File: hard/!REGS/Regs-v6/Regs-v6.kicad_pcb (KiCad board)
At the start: 2 copper layers, 160 x 99.1 mm, 60 parts, among them J1 Conn_01x15_Female, J10 Conn_01x01_Male, J11 Conn_01x03_Male, J12 Conn_01x01_Male, J13 Conn_01x01_Male, J14 Conn_01x01_Male, J15 Conn_01x01_Male, J16 Screw_Terminal_01x02, J17 Conn_01x09_Male, J18 Conn_01x09_Male, J19 Conn_01x01_Male, J2 Conn_01x15_Female, J20 Conn_01x01_Male, J21 Conn_01x01_Male, J22 Conn_01x01_Male, J23 Conn_01x01_Male, J24 Conn_01x01_Male, J3 Conn_01x15_Female, J4 Conn_01x15_Female, J5 Conn_01x15_Female, J6 Conn_01x15_Female, J7 Conn_01x15_Female, J8 Conn_01x15_Female, J9 Conn_01x01_Male, Q1 IRLML5203, U1 REG_CNT, U10 REG_CNT, U11 REG_CNT, U12 REG_CNT, U13 74LS139, U14 74HC00, U15 MUX2-1, U16 REG_CNT, U17 REG_CNT, U18 REG_CNT, U19 REG_CNT, U2 REG_CNT, U3 REG_CNT, U4 REG_CNT, U5 REG_CNT, U6 REG_CNT, U7 REG_CNT, U8 REG_CNT, U9 REG_CNT

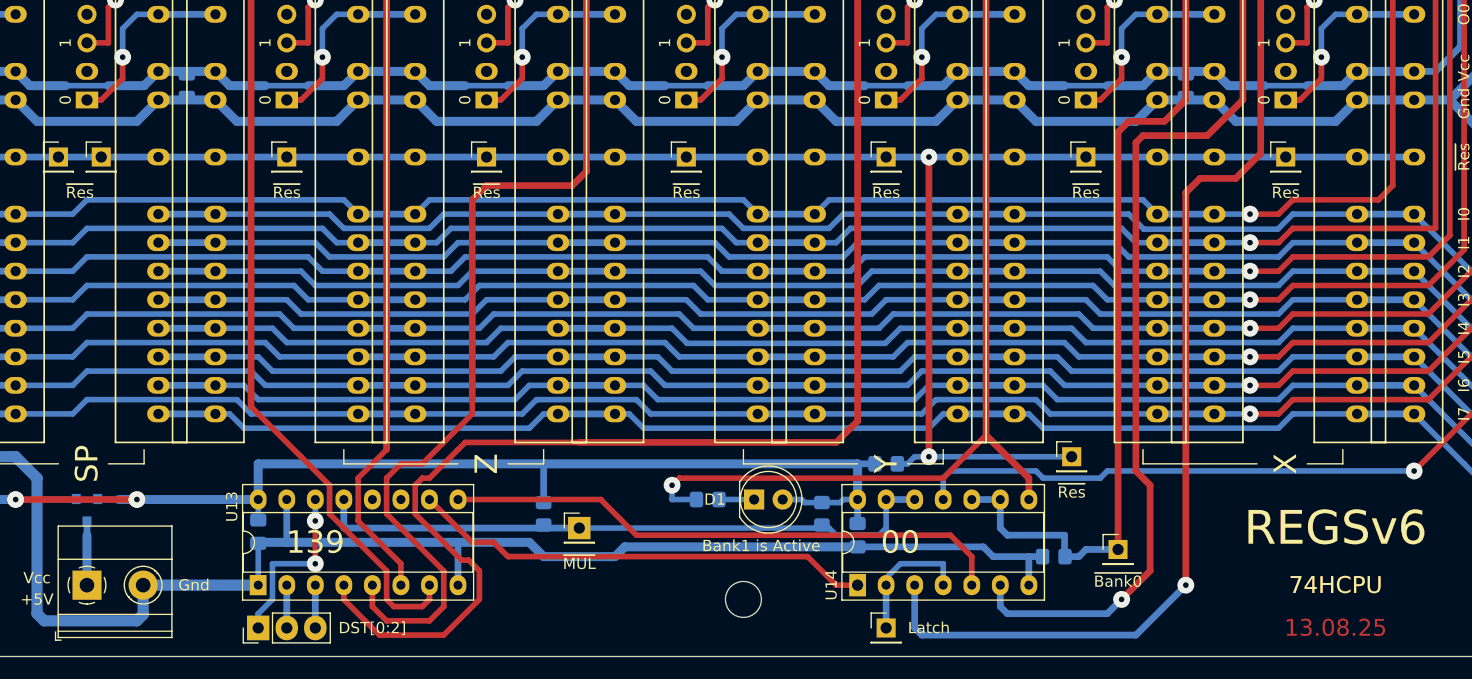
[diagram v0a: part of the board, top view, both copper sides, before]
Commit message: Fix label name
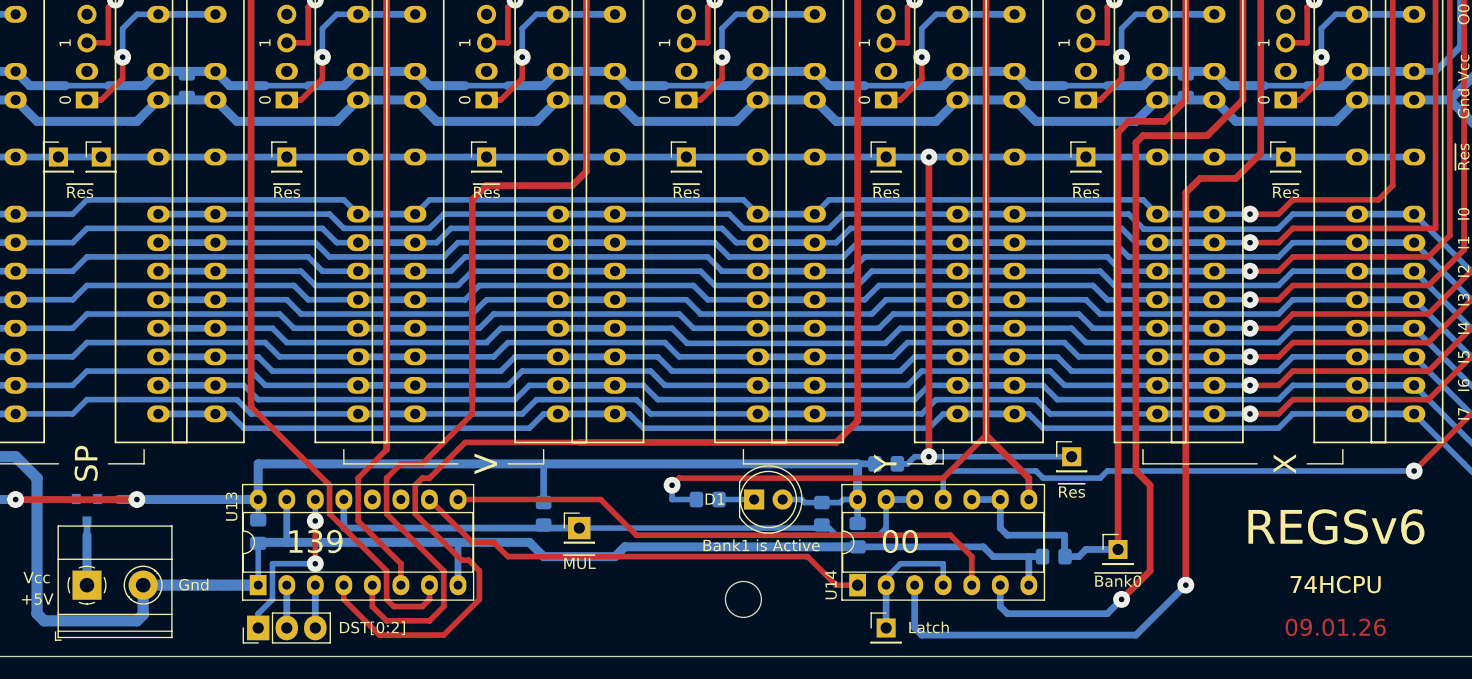
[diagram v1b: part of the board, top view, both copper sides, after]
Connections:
- net /~Bank0 renamed /~{Bank0}
- net /~Bank1 renamed /~{Bank1}
- net /~H renamed /~{H}
- net /~L renamed /~{L}
- net /~MUL renamed /~{MUL}
- net /~R0 renamed /~{R0}
- net /~R1 renamed /~{R1}
- net /~R2 renamed /~{R2}
- net /~R3 renamed /~{R3}
- net /~Res renamed /~{Res}
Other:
- net class Default removed
- board text added: "09.01.26"
- board text added: "V"
- board text added: "~{Bank0}"
- board text added: "~{CS}"
- board text added: "~{Col}"
- board text added: "~{MUL}"
- board text added: "~{Res}"
- board text added: "~{Row}"
- board text removed: "13.08.25"
- board text removed: "Z"
- board text removed: "~Bank0"
- board text removed: "~CS"
- board text removed: "~Col"
- board text removed: "~MUL"
- board text removed: "~Res"
- board text removed: "~Row"

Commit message: Regs v6.1
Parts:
- added J2: Conn_01x22_Socket, Connector_PinSocket_2.54mm:PinSocket_1x22_P2.54mm_Vertical, F.Cu at (183.5, 21.6)
- added J3: Conn_01x22_Socket, Connector_PinSocket_2.54mm:PinSocket_1x22_P2.54mm_Vertical, F.Cu at (188.0, 23.7)
- added J4: Conn_01x22_Socket, Connector_PinSocket_2.54mm:PinSocket_1x22_P2.54mm_Vertical, F.Cu at (192.6, 23.7)
- added J5: Conn_01x22_Socket, Connector_PinSocket_2.54mm:PinSocket_1x22_P2.54mm_Vertical, F.Cu at (197.2, 23.7)
- added J6: Conn_01x22_Socket, Connector_PinSocket_2.54mm:PinSocket_1x22_P2.54mm_Vertical, F.Cu at (201.8, 23.7)
- added J7: Conn_01x22_Socket, Connector_PinSocket_2.54mm:PinSocket_1x22_P2.54mm_Vertical, F.Cu at (206.4, 23.7)
- added J8: Conn_01x22_Socket, Connector_PinSocket_2.54mm:PinSocket_1x22_P2.54mm_Vertical, F.Cu at (211.0, 23.7)
- J1: value Conn_01x15_Female -> Conn_01x22_Socket; footprint Connector_PinSocket_2.54mm:PinSocket_1x15_P2.54mm_Vertical -> Connector_PinSocket_2.54mm:PinSocket_1x22_P2.54mm_Vertical
- moved J1 8.89 mm to (141.0, 71.1)
- moved J10 2.54 mm to (143.5, 67.3)
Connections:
- J1 pad 10: Net-(J1-Pad10) -> /R0.3
- J1 pad 11: /R0.5 -> unconnected-(J1-Pin_11-Pad11)
- J1 pad 12: Net-(J1-Pad12) -> unconnected-(J1-Pin_12-Pad12)
- J1 pad 13: /R0.6 -> /R0.4
- J1 pad 14: Net-(J1-Pad14) -> unconnected-(J1-Pin_14-Pad14)
- J1 pad 15: /R0.7 -> unconnected-(J1-Pin_15-Pad15)
- J1 pad 2: Net-(J1-Pad2) -> unconnected-(J1-Pin_2-Pad2)
- J1 pad 3: /R0.1 -> unconnected-(J1-Pin_3-Pad3)
- J1 pad 4: Net-(J1-Pad4) -> /R0.1
- J1 pad 5: /R0.2 -> unconnected-(J1-Pin_5-Pad5)
- J1 pad 6: Net-(J1-Pad6) -> unconnected-(J1-Pin_6-Pad6)
- J1 pad 7: /R0.3 -> /R0.2
- J1 pad 8: Net-(J1-Pad8) -> unconnected-(J1-Pin_8-Pad8)
- J1 pad 9: /R0.4 -> unconnected-(J1-Pin_9-Pad9)
- U13 pad 11: Net-(U13-Pad11) -> unconnected-(U13B-O1-Pad11)
- U13 pad 12: Net-(U13-Pad12) -> unconnected-(U13B-O0-Pad12)
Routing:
- net /R0.0: track 17.2 -> 26.5 mm, vias 1 -> 0
- net /R0.7: track 19.4 -> 27.9 mm, vias 1 -> 0
- net /R0.6: track 17.2 -> 23.9 mm, vias 1 -> 0
- net /R0.1: track 15.4 -> 20.6 mm, vias 1 -> 0
- net /R0.2: track 12.5 -> 15.5 mm, vias 1 -> 0
- net /R0.5: track 15.4 -> 18.1 mm, vias 1 -> 0
- net /~{Bank0}: track 259.5 -> 260.6 mm
- net VCC: track 326.4 -> 327.4 mm
- net /~{L}: track 233.1 -> 232.5 mm
- net /~{R0}: track 191.1 -> 191.6 mm
- net /R0.4: track 12.5 -> 13.0 mm, vias 1 -> 0
- net /R0.3: track 11.4 -> 12.0 mm, vias 1 -> 0
- net GND: track 402.3 -> 402.8 mm
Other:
- board text added: "23.02.26"
- board text added: "REGSv6.1"
- board text removed: "09.01.26"
- board text removed: "REGSv6"

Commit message: Regs v6.1 in work
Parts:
- removed the J2 at (123.2, 62.2)
- removed the J3 at (105.4, 62.2)
- removed the J4 at (87.6, 62.2)
- removed the J5 at (69.8, 62.2)
- removed the J6 at (52.1, 62.2)
- removed the J7 at (34.3, 62.2)
- removed the J8 at (16.5, 62.2)
- J2, J3, J4, J5, J6, J7, J8: moved to B.Cu
- moved J8 201.8 mm to (16.5, 77.5)
- moved J7 180.3 mm to (34.3, 77.5)
- moved J6 159.1 mm to (52.1, 77.5)
- moved J5 138.3 mm to (69.8, 77.5)
- moved J4 117.9 mm to (87.6, 77.5)
- moved J11 116.9 mm to (62.2, -6.97), turned to -90 degrees
- moved U13 109.3 mm to (62.2, -3.17), turned to -90 degrees
- moved R5 103.2 mm to (36.8, 3.19), turned to -90 degrees
- moved C3 99.9 mm to (62.2, 1.60), turned to 90 degrees
- moved J3 98.6 mm to (105.4, 77.5)
- moved J2 82.2 mm to (123.2, 77.5)
- moved J15 44.4 mm to (61.0, 109.2)
- moved J14 40.6 mm to (85.6, 105.8)
- moved R7 38.7 mm to (81.8, 106.2), turned to -90 degrees
- moved R6 36.5 mm to (69.2, 99.7)
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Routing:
- net GND: track 402.8 -> 298.9 mm
- net /~{Bank0}: track 260.6 -> 179.8 mm, vias 13 -> 10
- net VCC: track 327.4 -> 247.8 mm
- net /~{R0}: track 191.6 -> 124.2 mm
- net /~{R1}: track 148.3 -> 87.6 mm
- net /~{H}: track 220.9 -> 164.3 mm, vias 2 -> 1
- net Net-(U15-S): track 116.4 -> 61.0 mm, vias 1 -> 0
- net Net-(U13B-O3): track 50.4 -> 2.54 mm
- net /~{L}: track 232.5 -> 194.5 mm, vias 2 -> 1
- net Net-(U13B-O2): track 41.3 -> 5.50 mm
- net /~{R3}: track 119.7 -> 95.0 mm
- net /H7: track 174.8 -> 159.5 mm
- net /L6: track 138.6 -> 124.2 mm
- net /L5: track 138.6 -> 124.2 mm
- net /L4: track 138.6 -> 124.3 mm
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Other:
- board text added: "Добавить конденсаторов между каждой парой регистров!"

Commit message: Regs-v6.1 in work
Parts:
- moved J21 0.63 mm to (108.0, 73.7)
- moved J23 0.63 mm to (125.7, 73.7)
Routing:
- net /R1.0: track 13.2 -> 26.5 mm, vias 1 -> 0
- net /H3: track 166.9 -> 179.6 mm
- net /R3.7: track 16.8 -> 27.9 mm, vias 1 -> 0
- net /R2.7: track 16.8 -> 27.9 mm, vias 1 -> 0
- net /R1.7: track 16.8 -> 27.9 mm, vias 1 -> 0
- net /R2.6: track 12.6 -> 23.5 mm, vias 1 -> 0
- net /H4: track 168.7 -> 179.6 mm
- net /R2.0: track 15.9 -> 26.5 mm, vias 1 -> 0
- net /H5: track 170.5 -> 179.6 mm
- net /R2.5: track 9.42 -> 18.5 mm, vias 1 -> 0
- net /R3.6: track 15.9 -> 23.5 mm, vias 1 -> 0
- net /R1.6: track 15.9 -> 23.5 mm, vias 1 -> 0
- net /R2.1: track 13.5 -> 20.6 mm, vias 1 -> 0
- net /R1.1: track 13.5 -> 20.6 mm, vias 1 -> 0
- net /R2.2: track 8.89 -> 15.5 mm, vias 1 -> 0
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
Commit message: Regs v6.1 in work
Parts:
- removed R2: 10k, Resistor_SMD:R_0805_2012Metric_Pad1.20x1.40mm_HandSolder
- moved J11 141.2 mm to (141.6, 109.9), turned to 180 degrees
- moved U13 127.9 mm to (134.6, 102.2)
- moved C3 123.0 mm to (127.0, 106.2)
- moved R5 103.9 mm to (63.5, 103.6), turned to 90 degrees
- moved J13 0.64 mm to (90.2, 73.7)
- moved J19 0.64 mm to (36.8, 73.7)
- moved J24 0.64 mm to (72.4, 73.7)
- moved J20 0.63 mm to (54.6, 73.7)
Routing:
- net /~{L}: track 194.5 -> 169.8 mm
- net /~{MUL}: track 45.5 -> 22.0 mm
- net /R6.7: track 5.08 -> 27.9 mm
- net /R6.0: track 5.08 -> 26.5 mm
- net /R5.7: track 8.25 -> 27.9 mm
- net /H0: track 159.1 -> 177.7 mm
- net /R6.6: track 5.08 -> 23.5 mm
- net /R6.1: track 5.08 -> 20.6 mm
- net /R5.0: track 11.3 -> 26.5 mm
- net /DST[0]: track 14.5 -> 0.00 mm, vias 2 -> 0
- net /H2: track 165.1 -> 179.6 mm
- net /H1: track 163.7 -> 177.6 mm
- net /L3: track 124.2 -> 136.0 mm
- net /L2: track 124.2 -> 136.0 mm
- net /L7: track 124.2 -> 136.0 mm
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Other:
- board text added: "11.03.26"
- board text removed: "23.02.26"

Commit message: Regs-v6.1 in work
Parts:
- R7: moved to F.Cu
- moved J12 27.6 mm to (83.2, 109.9)
- moved J14 26.2 mm to (59.7, 109.9)
- moved J15 23.3 mm to (83.2, 102.2)
- moved R5 22.5 mm to (85.4, 108.6)
- moved R7 22.4 mm to (59.4, 104.7), turned to 0 degrees
- moved R6 19.8 mm to (87.6, 107.0), turned to 90 degrees
- moved U14 14.3 mm to (78.7, 102.2), turned to -90 degrees
- moved J9 10.2 mm to (87.6, 109.9)
- moved D1 10.2 mm to (49.5, 108.6), turned to 180 degrees
- moved C3 10.2 mm to (116.8, 106.4)
- moved R1 6.72 mm to (54.9, 109.9), turned to 0 degrees
- moved Q1 2.61 mm to (35.6, 102.5)
- moved J11 1.27 mm to (140.3, 109.9)
- moved C4 0.68 mm to (67.3, 105.6), turned to 90 degrees
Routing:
- net GND: track 306.4 -> 424.6 mm
- net /~{Bank0}: track 173.9 -> 249.6 mm
- net VCC: track 245.9 -> 316.6 mm
- net /~{MUL}: track 22.0 -> 59.6 mm
- net /~{Bank1}: track 226.1 -> 204.9 mm, vias 2 -> 1
- net /DST[1]: track 0.00 -> 18.5 mm
- net /DST[0]: track 0.00 -> 13.4 mm
- net /DST[2]: track 0.00 -> 13.1 mm
- net Net-(U13B-O2): track 5.50 -> 0.00 mm
- net Net-(U13B-O3): track 2.54 -> 0.00 mm
- net /~{Res}: track 171.7 -> 169.2 mm, vias 2 -> 1
- net Net-(D1-K): track 3.13 -> 4.88 mm
- net Net-(U15-S): track 61.0 -> 59.3 mm
- net Net-(J16-Pin_1): track 3.76 -> 5.32 mm
- net /Latch: track 17.1 -> 16.3 mm

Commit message: Regs v6.1 in work
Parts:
- R6: moved to F.Cu
- moved J9 7.65 mm to (87.0, 102.2)
- moved R6 4.82 mm to (82.8, 106.7), turned to 180 degrees
- moved J12 0.64 mm to (82.5, 109.9)
- moved R7 0.53 mm to (59.7, 105.1), turned to 90 degrees
- moved R5 0.32 mm to (85.1, 108.6)
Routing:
- net /~{R3}: track 95.0 -> 169.6 mm
- net /~{R2}: track 93.5 -> 135.5 mm
- net /~{H}: track 158.6 -> 189.2 mm
- net /~{R0}: track 124.2 -> 99.6 mm
- net /H7: track 159.5 -> 183.4 mm
- net /~{L}: track 169.8 -> 193.4 mm
- net /~{Bank1}: track 204.9 -> 227.6 mm
- net VCC: track 316.6 -> 333.6 mm
- net /H6: track 163.3 -> 179.6 mm
- net /~{R1}: track 87.6 -> 99.6 mm, vias 1 -> 0
- net Net-(U15-S): track 59.3 -> 54.0 mm
- net /~{Bank0}: track 249.6 -> 254.4 mm
- net /DST[2]: track 13.1 -> 16.6 mm
- net /DST[1]: track 18.5 -> 15.6 mm
- net GND: track 424.6 -> 421.7 mm
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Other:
- board text added: "18.03.26"
- board text removed: "11.03.26"

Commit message: Regs v6.1 is almost ready!
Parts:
- moved R6 3.55 mm to (86.0, 105.1)
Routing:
- net Net-(U15-S): track 54.0 -> 178.3 mm, vias 0 -> 2
- net Net-(U13B-O2): track 0.00 -> 52.4 mm
- net Net-(U13B-O3): track 0.00 -> 51.8 mm, vias 0 -> 1
- net /~{Res}: track 171.1 -> 163.4 mm
- net VCC: track 333.6 -> 331.2 mm, vias 2 -> 3
- net GND: track 421.7 -> 423.5 mm
- net /Latch: track 16.3 -> 17.4 mm
- net /L3: track 136.9 -> 136.0 mm
- net /H1: track 177.6 -> 178.4 mm
- net /~{R3}: track 169.6 -> 170.2 mm
